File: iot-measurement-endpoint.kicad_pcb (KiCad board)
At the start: 4 copper layers, 55.3 x 39.5 mm, 97 parts, among them K1 Con_01x02, M1 Motor_DC, P1 USB_C_Plug_USB2.0, Q2 DMC2053UVT, Q3 DMC2053UVT, SW1 KMR232NG ULC LFS, SW2 KMR232NG ULC LFS, SW3 SW_Push, U1 CH330N, U2 ESP32-C3-WROOM-02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

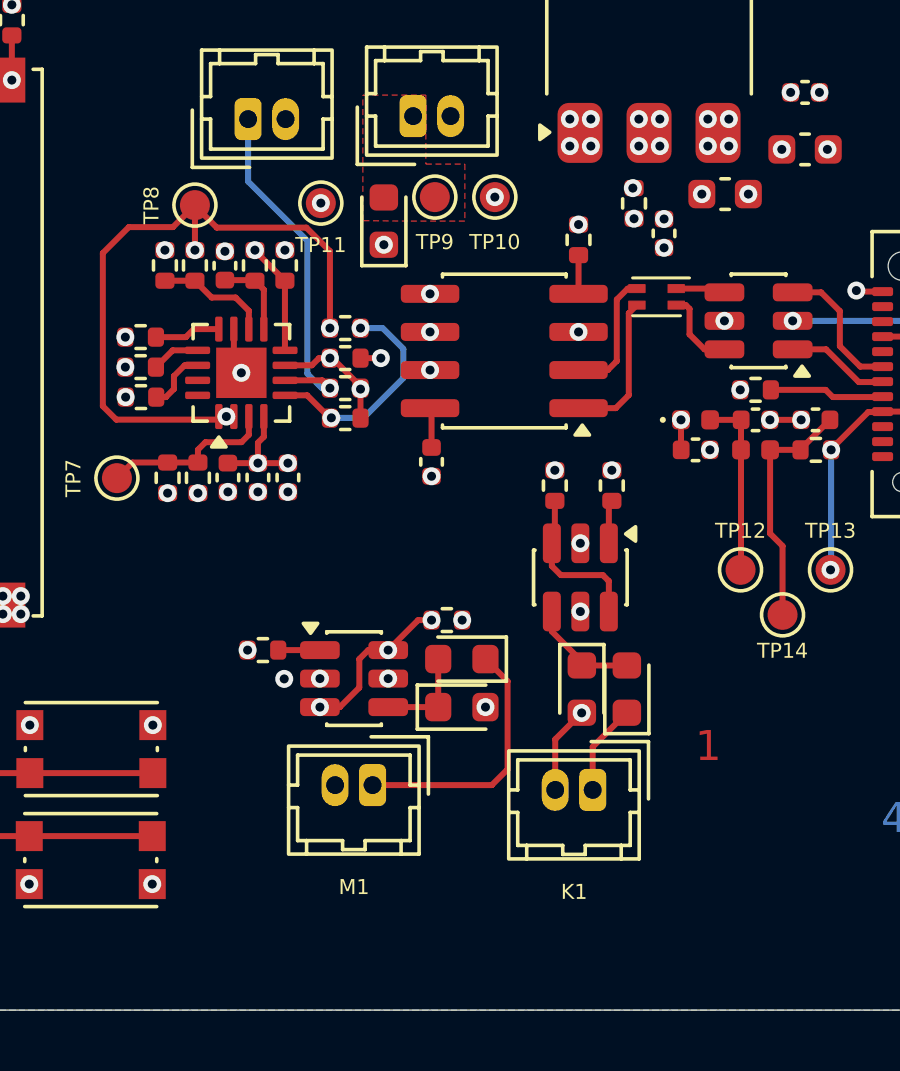
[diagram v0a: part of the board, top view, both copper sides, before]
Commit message: Fixing power planes for motor and valve outputs
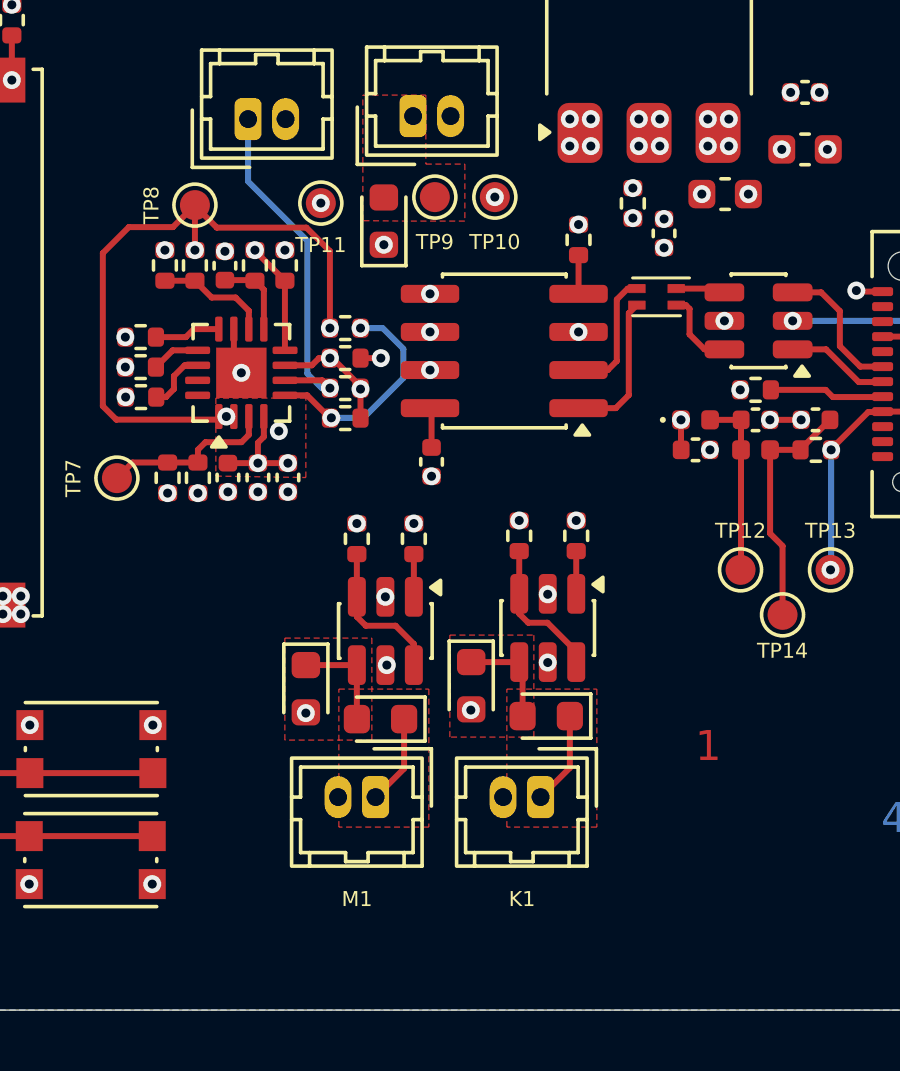
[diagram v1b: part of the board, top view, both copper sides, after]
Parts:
- moved R7 6.25 mm to (93.9, 133.3), turned to 90 degrees
- moved D4 5.24 mm to (90.3, 138.3), turned to -90 degrees
- moved R5 4.04 mm to (92.0, 133.3), turned to 90 degrees
- moved D5 3.69 mm to (95.8, 138.2)
- moved D8 3.37 mm to (92.8, 139.3)
- moved D7 2.83 mm to (98.3, 139.2), turned to 180 degrees
- moved R6 2.05 mm to (97.4, 133.2)
- moved R8 2.05 mm to (99.3, 133.2)
- moved Q3 2.01 mm to (98.4, 136.3)
- moved Q2 1.90 mm to (93.0, 136.4), turned to -90 degrees
- moved K1 1.75 mm to (98.1, 141.9)
- moved M1 0.41 mm to (92.6, 141.9)
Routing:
- net Net-(D8-K): track 8.70 -> 2.99 mm
- net SW0: track 28.0 -> 32.0 mm
- net GND: track 6.76 -> 3.81 mm
- net Net-(Q2A-D): track 5.48 -> 5.07 mm, vias 3 -> 0
- net +6V: vias 13 -> 12
- net +3.3V: vias 22 -> 23
- added copper zone on F.Cu, net +3.3V
- added copper zone on F.Cu, net Net-(D4-K)
- added copper zone on F.Cu, net Net-(D5-K)
- added copper zone on F.Cu, net Net-(D7-K)
- added copper zone on F.Cu, net Net-(D8-K)

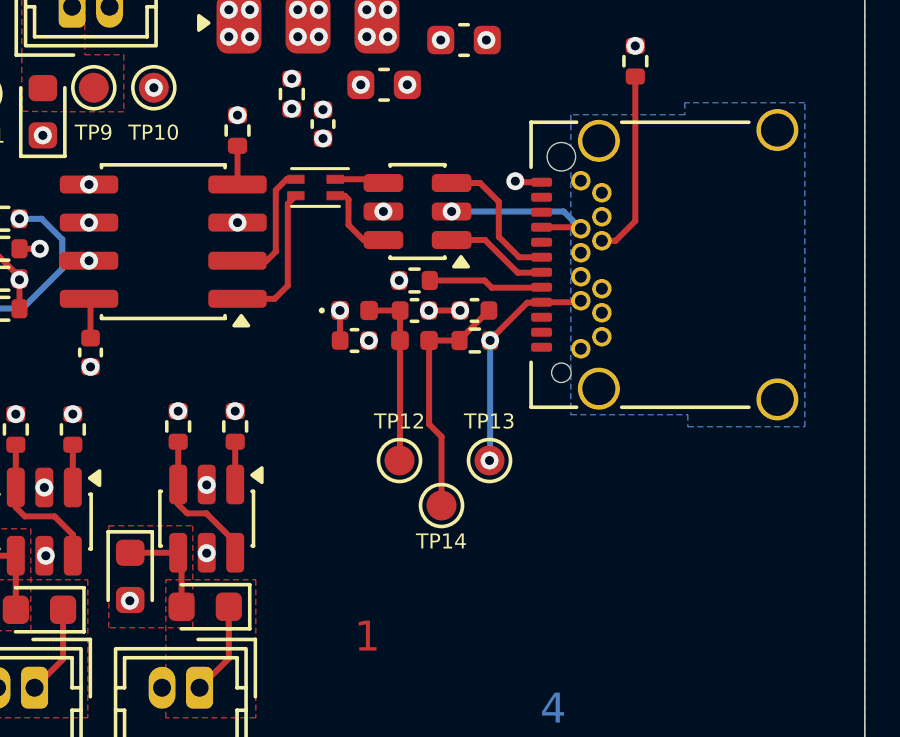
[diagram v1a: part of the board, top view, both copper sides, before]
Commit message: Fixing filter response to put loads at 10 MHz signals and 1 GHz signals (low pass RC and ferrite) at DC power supply (rejecting high frequency noise in the power supply).
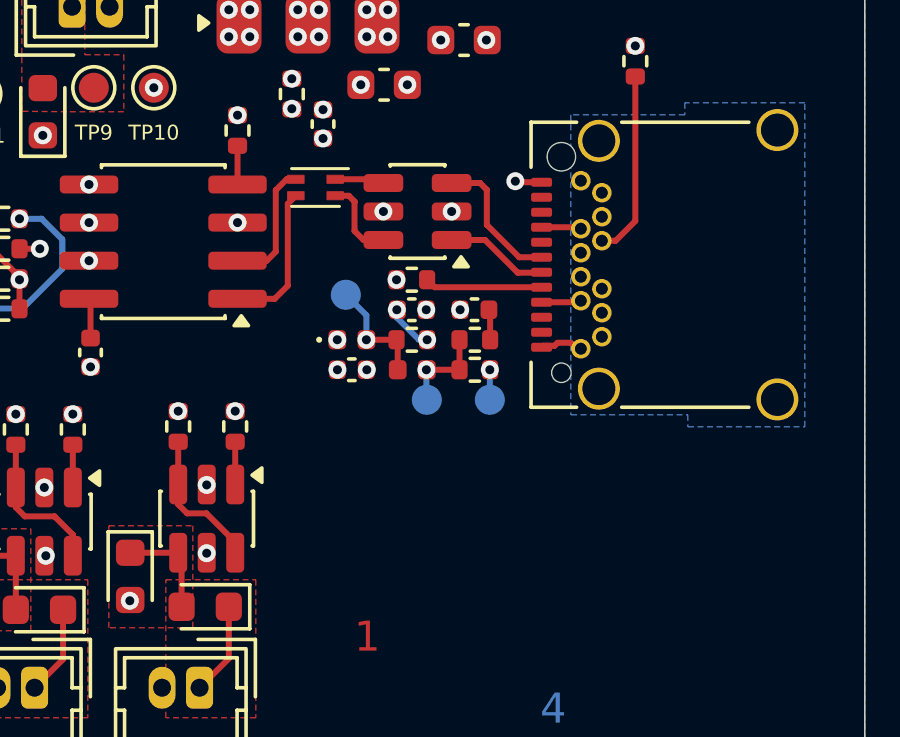
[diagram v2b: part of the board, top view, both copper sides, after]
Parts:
- added R36: 500R, Resistor_SMD:R_0402_1005Metric, F.Cu at (105.2, 130.3)
- added R37: 0R, Resistor_SMD:R_0402_1005Metric, F.Cu at (107.3, 130.3)
- C13: value 100pF -> 1pF
- C14: value 100pF -> 470pF
- FB1: value BLM15AG121SN1D -> AIML-0402-1R0
- R34, R35: value 0R -> 180R
- TP12, TP13, TP14: moved to B.Cu
- moved TP12 5.81 mm to (103.0, 128.8), turned to 180 degrees
- moved TP14 3.56 mm to (105.7, 132.3), turned to 180 degrees
- moved TP13 2.03 mm to (107.8, 132.3), turned to 180 degrees
- moved C1 0.98 mm to (103.2, 131.3)
- moved D2 0.98 mm to (103.2, 130.3)
- moved FB1 0.98 mm to (105.2, 131.3)
- moved TH1 0.98 mm to (107.3, 131.3)
- moved C14 0.09 mm to (105.2, 129.3)
- moved R28 0.09 mm to (105.2, 128.3)
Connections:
- C13 pad 1: /USB Connector/VBUS_PROTECTED -> Net-(C13-Pad1)
- C14 pad 1: /USB Connector/VBUS_FILTERED -> Net-(C14-Pad1)
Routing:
- net /USB Connector/VBUS: track 17.0 -> 7.28 mm, vias 3 -> 2
- net /USB Connector/VBUS_PROTECTED: track 8.09 -> 3.26 mm, vias 0 -> 1
- net /USB Connector/VBUS_FILTERED: track 6.04 -> 3.84 mm, vias 0 -> 1
- net Net-(C14-Pad1): track 0.00 -> 1.70 mm, vias 0 -> 2
- net Net-(C13-Pad1): track 0.00 -> 1.07 mm
- net +6V: track 1.00 -> 0.01 mm, vias 12 -> 13
- added copper zone on In2.Cu, net /USB Connector/VBUS

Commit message: Routing improvement
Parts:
- removed R14: 0R, Resistor_SMD:R_0402_1005Metric
- added NT1: NetTie_2, NetTie:NetTie-2_SMD_Pad0.5mm, F.Cu at (102.5, 122.1)
- moved TP7 7.80 mm to (91.8, 130.5), turned to 180 degrees
- moved TP11 7.55 mm to (98.3, 123.0)
- moved TP8 6.96 mm to (82.7, 127.9), turned to 180 degrees
- moved C8 6.76 mm to (91.7, 124.8), turned to 0 degrees
- moved R21 6.62 mm to (89.8, 122.9), turned to -90 degrees
- moved R19 6.53 mm to (91.8, 128.8), turned to 180 degrees
- moved R20 6.37 mm to (86.2, 122.9), turned to -90 degrees
- moved C9 6.24 mm to (91.7, 125.8), turned to 0 degrees
- moved R22 6.16 mm to (88.6, 122.9), turned to -90 degrees
- moved R18 6.12 mm to (91.8, 127.8), turned to 0 degrees
- moved R23 6.07 mm to (87.4, 122.9), turned to 90 degrees
- moved C20 6.01 mm to (91.7, 126.8), turned to 0 degrees
- moved R27 4.98 mm to (84.7, 124.9), turned to 180 degrees
- moved R26 4.81 mm to (84.7, 128.9), turned to 0 degrees
- moved R33 4.40 mm to (89.1, 129.7), turned to 90 degrees
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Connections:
- R32 pad 1: Net-(U2-IO19) -> /Microcontroller/IO0
- U2 pad 14: Net-(U2-IO19) -> FREQ
- U2 pad 18: FREQ -> /Microcontroller/IO0
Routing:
- net FREQ: track 33.2 -> 21.3 mm
- net Net-(U3B--): track 11.9 -> 6.33 mm
- net /Microcontroller/IO0: track 0.00 -> 5.12 mm, vias 0 -> 2
- net TXD: track 21.6 -> 24.2 mm
- net RXD: track 19.7 -> 22.2 mm
- net REF_FREQ: track 27.5 -> 25.2 mm
- net /Sensor/SPLIT: track 23.2 -> 21.3 mm
- net /USB Connector/USB_D+_FILTERED: track 4.97 -> 3.34 mm
- net SW0: track 32.0 -> 30.4 mm
- net Net-(U2-IO19): track 1.49 -> 0.00 mm, vias 1 -> 0
- net /USB Connector/USB_D-_FILTERED: track 4.27 -> 2.84 mm
- net Net-(U3B-+): track 7.50 -> 8.78 mm
- net /USB Connector/USB_D+_PROTECTED: track 2.80 -> 1.61 mm
- net SW1: track 34.7 -> 33.7 mm
- net /USB Connector/USB_D-_PROTECTED: track 1.66 -> 2.58 mm
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
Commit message: Unifying 3.3V plane with the regulator output (removing net tie)
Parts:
- removed NT1: NetTie_2, NetTie:NetTie-2_SMD_Pad0.5mm
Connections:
- U4 pad 2: Net-(U4-VO) -> +3.3V
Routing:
- net Net-(U4-VO): vias 15 -> 0
- net +3.3V: vias 23 -> 36
- removed copper zone on In2.Cu, net Net-(U4-VO)
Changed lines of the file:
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@@
 		)
 	)
-	(footprint "NetTie:NetTie-2_SMD_Pad0.5mm"
-		(layer "F.Cu")
-		(at 102.5 122.1 -90)
-		(descr "Net tie, 2 pin, 0.5mm square SMD pads")
-		(tags "net tie")
-		(property "Reference" "NT1"
-			(at 0 -1.2 90)
-			(layer "F.SilkS")
-			(hide yes)
-			(effects
-				(font
-					(size 1 1)
-					(thickness 0.15)
-				)
-			)
-		)
-		(property "Value" "NetTie_2"
-			(at 0 1.2 90)
-			(layer "F.Fab")
-			(hide yes)
-			(effects
-				(font
-					(size 1 1)
-					(thickness 0.15)
-				)
-			)
-		)
-		(property "Datasheet" ""
-			(at 0 0 270)
-			(unlocked yes)
-			(layer "F.Fab")
-			(hide yes)
-			(effects
-				(font
-					(size 1.27 1.27)
-					(thickness 0.15)
-				)
-			)
-		)
-		(property "Description" "Net tie, 2 pins"
-			(at 0 0 270)
-			(unlocked yes)
-			(layer "F.Fab")
-			(hide yes)
-			(effects
-				(font
-					(size 1.27 1.27)
-					(thickness 0.15)
-				)
-			)
-		)
-		(property ki_fp_filters "Net*Tie*")
-		(sheetname "/3.3V Regulator/")
-		(sheetfile "3.3V Regulator.kicad_sch")
-		(units
-			(unit
-				(name "A")
-				(pins "1" "2")
-			)
-		)
-		(attr exclude_from_bom allow_missing_courtyard)
-		(net_tie_pad_groups "1, 2")
-		(duplicate_pad_numbers_are_jumpers no)
-		(fp_poly
-			(pts
-				(xy -0.5 -0.25) (xy 0.5 -0.25) (xy 0.5 0.25) (xy -0.5 0.25)
-			)
-			(stroke
-				(width 0)
-				(type solid)
-			)
-			(fill yes)
-			(layer "F.Cu")
-		)
-		(pad "1" smd circle
-			(at -0.5 0 270)
-			(size 0.5 0.5)
-			(layers "F.Cu")
-			(net "Net-(U4-VO)")
-			(pinfunction "1_1")
-			(pintype "passive")
-		)
-		(pad "2" smd circle
-			(at 0.5 0 270)
-			(size 0.5 0.5)
-			(layers "F.Cu")
-			(net "+3.3V")
-			(pinfunction "2_2")
-			(pintype "passive")
-		)
-		(embedded_fonts no)
-	)
 	(footprint "Resistor_SMD:R_0402_1005Metric"
 		(layer "F.Cu")
@@
 			(layers "F.Cu" "F.Mask" "F.Paste")
 			(roundrect_rratio 0.25)
-			(net "Net-(U4-VO)")
+			(net "+3.3V")
 			(pinfunction "VO_2")
 			(pintype "power_out")
@@
 			(layers "F.Cu" "F.Mask" "F.Paste")
 			(roundrect_rratio 0.25)
-			(net "Net-(U4-VO)")
+			(net "+3.3V")
 			(pinfunction "VO_2")
 			(pintype "power_out")
@@
 	)
 	(via
+		(at 101 113.8)
+		(size 0.6)
+		(drill 0.3)
+		(layers "F.Cu" "B.Cu")
+		(net "+3.3V")
+	)
+	(via
 		(at 68.2 139.22)
 		(size 0.6)
@@
 	)
 	(via
+		(at 101.4 119.3)
+		(size 0.6)
+		(drill 0.3)
+		(layers "F.Cu" "B.Cu")
+		(net "+3.3V")
+	)
+	(via
+		(at 102.4 113.1)
+		(size 0.6)
+		(drill 0.3)
+		(layers "F.Cu" "B.Cu")
+		(net "+3.3V")
+	)
+	(via
 		(at 99.9 122.58)
 		(size 0.6)
@@
 	)
 	(via
+		(at 102.4 113.8)
+		(size 0.6)
+		(drill 0.3)
+		(layers "F.Cu" "B.Cu")
+		(net "+3.3V")
+	)
+	(via
 		(at 101.2125 123.3875)
 		(size 0.6)
@@
 	)
 	(via
+		(at 102.1 120.2)
+		(size 0.6)
+		(drill 0.3)
+		(layers "F.Cu" "B.Cu")
+		(net "+3.3V")
+	)
+	(via
+		(at 102.1 119.3)
+		(size 0.6)
+		(drill 0.3)
+		(layers "F.Cu" "B.Cu")
+		(net "+3.3V")
+	)
+	(via
 		(at 71.09 139.4)
 		(size 0.6)
@@
 	)
 	(via
+		(at 100.3 113.8)
+		(size 0.6)
+		(drill 0.3)
+		(layers "F.Cu" "B.Cu")
+		(net "+3.3V")
+	)
+	(via
+		(at 101.7 113.1)
+		(size 0.6)
+		(drill 0.3)
+		(layers "F.Cu" "B.Cu")
+		(net "+3.3V")
+	)
+	(via
 		(at 98.3 123)
 		(size 0.6)
@@
 	)
 	(via
+		(at 100.3 113.1)
+		(size 0.6)
+		(drill 0.3)
+		(layers "F.Cu" "B.Cu")
+		(net "+3.3V")
+	)
+	(via
 		(at 74.34 137.96)
 		(size 0.6)
@@
 	)
 	(via
+		(at 101.7 113.8)
+		(size 0.6)
+		(drill 0.3)
+		(layers "F.Cu" "B.Cu")
+		(net "+3.3V")
+	)
+	(via
+		(at 103.1 113.1)
+		(size 0.6)
+		(drill 0.3)
+		(layers "F.Cu" "B.Cu")
+		(net "+3.3V")
+	)
+	(via
 		(at 68.8 135.2)
 		(size 0.6)
@@
 	)
 	(via
+		(at 101.4 120.2)
+		(size 0.6)
+		(drill 0.3)
+		(layers "F.Cu" "B.Cu")
+		(net "+3.3V")
+	)
+	(via
+		(at 103.1 113.8)
+		(size 0.6)
+		(drill 0.3)
+		(layers "F.Cu" "B.Cu")
+		(net "+3.3V")
+	)
+	(via
 		(at 98.3625 135.14)
 		(size 0.6)
@@
 	)
 	(via
-		(at 102.5 122.6)
+		(at 101 113.1)
 		(size 0.6)
 		(drill 0.3)
@@
 		(net "SW1")
 	)
-	(via
-		(at 101 113.8)
-		(size 0.6)
-		(drill 0.3)
-		(layers "F.Cu" "B.Cu")
-		(net "Net-(U4-VO)")
-	)
-	(via
-		(at 101.4 119.3)
-		(size 0.6)
-		(drill 0.3)
-		(layers "F.Cu" "B.Cu")
-		(net "Net-(U4-VO)")
-	)
-	(via
-		(at 102.4 113.1)
-		(size 0.6)
-		(drill 0.3)
-		(layers "F.Cu" "B.Cu")
-		(net "Net-(U4-VO)")
-	)
-	(via
-		(at 102.4 113.8)
-		(size 0.6)
-		(drill 0.3)
-		(layers "F.Cu" "B.Cu")
-		(net "Net-(U4-VO)")
-	)
-	(via
-		(at 102.5 121.6)
-		(size 0.6)
-		(drill 0.3)
-		(layers "F.Cu" "B.Cu")
-		(net "Net-(U4-VO)")
-	)
-	(via
-		(at 102.1 120.2)
-		(size 0.6)
-		(drill 0.3)
-		(layers "F.Cu" "B.Cu")
-		(net "Net-(U4-VO)")
-	)
-	(via
-		(at 102.1 119.3)
-		(size 0.6)
-		(drill 0.3)
-		(layers "F.Cu" "B.Cu")
-		(net "Net-(U4-VO)")
-	)
-	(via
-		(at 100.3 113.8)
-		(size 0.6)
-		(drill 0.3)
-		(layers "F.Cu" "B.Cu")
-		(net "Net-(U4-VO)")
-	)
-	(via
-		(at 101.7 113.1)
-		(size 0.6)
-		(drill 0.3)
-		(layers "F.Cu" "B.Cu")
-		(net "Net-(U4-VO)")
-	)
-	(via
-		(at 100.3 113.1)
-		(size 0.6)
-		(drill 0.3)
-		(layers "F.Cu" "B.Cu")
-		(net "Net-(U4-VO)")
-	)
-	(via
-		(at 101.7 113.8)
-		(size 0.6)
-		(drill 0.3)
-		(layers "F.Cu" "B.Cu")
-		(net "Net-(U4-VO)")
-	)
-	(via
-		(at 103.1 113.1)
-		(size 0.6)
-		(drill 0.3)
-		(layers "F.Cu" "B.Cu")
-		(net "Net-(U4-VO)")
-	)
-	(via
-		(at 101.4 120.2)
-		(size 0.6)
-		(drill 0.3)
-		(layers "F.Cu" "B.Cu")
-		(net "Net-(U4-VO)")
-	)
-	(via
-		(at 103.1 113.8)
-		(size 0.6)
-		(drill 0.3)
-		(layers "F.Cu" "B.Cu")
-		(net "Net-(U4-VO)")
-	)
-	(via
-		(at 101 113.1)
-		(size 0.6)
-		(drill 0.3)
-		(layers "F.Cu" "B.Cu")
-		(net "Net-(U4-VO)")
-	)
 	(segment
 		(start 107.64 126.975)
@@
 			)
 		)
-	)
-	(zone
-		(net "Net-(U4-VO)")
-		(layer "In2.Cu")
-		(hatch edge 0.5)
-		(priority 9)
-		(connect_pads yes
-			(clearance 0)
-		)
-		(min_thickness 0.25)
-		(fill yes
-			(thermal_gap 0.5)
-			(thermal_bridge_width 0.5)
-			(island_removal_mode 0)
-		)
-		(polygon
-			(pts
-				(xy 98.2 112.1) (xy 98.2 122.1) (xy 105.3 122.1) (xy 105.3 112.1)
-			)
-		)
